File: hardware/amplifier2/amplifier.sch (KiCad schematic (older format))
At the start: 130 parts, among them IC1 AD8331, IC2 ISL55210, IC3 LP38798, IC4 NC7SVU04, IC5 LTC2252, J1 0, P1 5V, P2 UART, P4 VGA - LNA, P5 LNA - SDR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

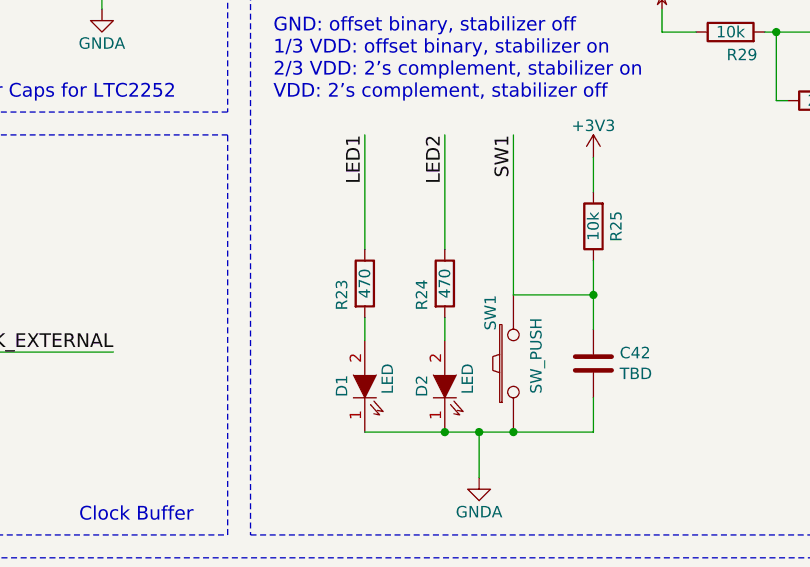
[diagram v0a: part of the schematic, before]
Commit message: Routed LDO, updated LED resistors, added resistor part numbers
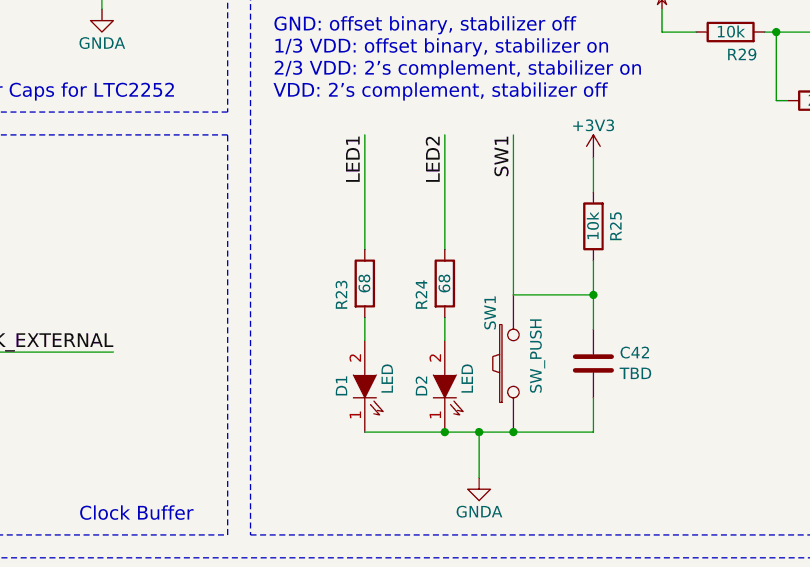
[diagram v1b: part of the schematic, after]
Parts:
- R23, R24: value 470 -> 68
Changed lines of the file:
@@
 P 7700 4250
 F 0 "R24" V 7600 4200 50  0000 C CNN
-F 1 "470" V 7700 4250 50  0000 C CNN
+F 1 "68" V 7700 4250 50  0000 C CNN
 F 2 "Resistors_SMD:R_0603" V 7630 4250 50  0001 C CNN
 F 3 "" H 7700 4250 50  0000 C CNN
@@
 P 7350 4250
 F 0 "R23" V 7250 4200 50  0000 C CNN
-F 1 "470" V 7350 4250 50  0000 C CNN
+F 1 "68" V 7350 4250 50  0000 C CNN
 F 2 "Resistors_SMD:R_0603" V 7280 4250 50  0001 C CNN
 F 3 "" H 7350 4250 50  0000 C CNN

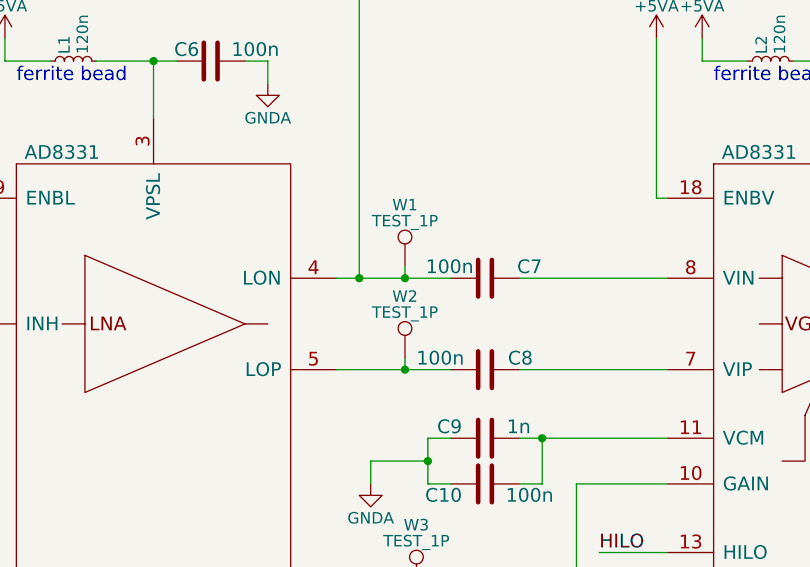
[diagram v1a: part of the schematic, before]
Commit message: everything done routing; removed obsolete testpins; needs groundplane checks and stitchings; needs mounting holes; maybe elaborate in schema
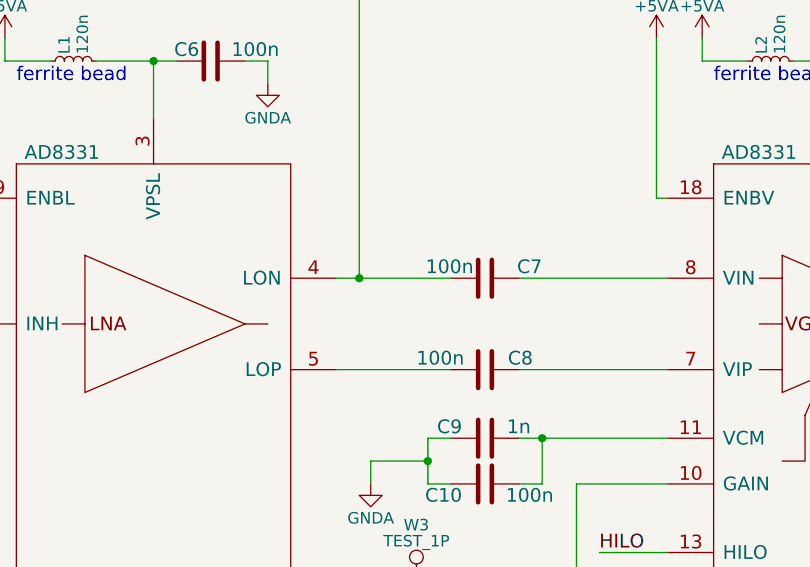
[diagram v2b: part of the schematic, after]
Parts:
- removed W1, W2: TEST_1P, Measurement_Points:Test_Point_Keystone_5005-5009_Compact, symbol TEST_1P
- C27: footprint Capacitors_SMD:C_0603 -> Capacitors_SMD:C_1210
- IC3: footprint (none) -> SDRfootprints:WSON12
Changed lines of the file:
@@
-$EndComp
-$Comp
-L TEST_1P W1
-U 1 1 580018C4
-P 3850 7450
-F 0 "W1" H 3850 7720 50  0000 C CNN
-F 1 "TEST_1P" H 3850 7650 50  0000 C CNN
-F 2 "Measurement_Points:Test_Point_Keystone_5005-5009_Compact" H 4050 7450 50  0001 C CNN
-F 3 "" H 4050 7450 50  0000 C CNN
-	1    3850 7450
-	1    0    0    -1
-$EndComp
-$Comp
-L TEST_1P W2
-U 1 1 58001975
-P 3850 7850
-F 0 "W2" H 3850 8120 50  0000 C CNN
-F 1 "TEST_1P" H 3850 8050 50  0000 C CNN
-F 2 "Measurement_Points:Test_Point_Keystone_5005-5009_Compact" H 4050 7850 50  0001 C CNN
-F 3 "" H 4050 7850 50  0000 C CNN
-	1    3850 7850
-	1    0    0    -1
 $EndComp
 $Comp
@@
 F 0 "C27" H 1565 1346 50  0000 L CNN
 F 1 "100u" H 1565 1255 50  0000 L CNN
-F 2 "Capacitors_SMD:C_0603" H 1488 1150 50  0001 C CNN
+F 2 "Capacitors_SMD:C_1210" H 1488 1150 50  0001 C CNN
 F 3 "" H 1450 1300 50  0000 C CNN
 	1    1450 1300
@@
 	8800 6050 8800 6500
 Connection ~ 8800 6150
-Wire Wire Line
-	3850 7450 3850 7500
-Connection ~ 3850 7500
-Wire Wire Line
-	3850 7850 3850 7900
-Connection ~ 3850 7900
 Wire Wire Line
 	9300 6150 9800 6150
@@
 F 0 "IC3" H 2875 2637 60  0000 C CNN
 F 1 "LP38798" H 2875 2531 60  0000 C CNN
-F 2 "" H 2900 1700 60  0001 C CNN
+F 2 "SDRfootprints:WSON12" H 2900 1700 60  0001 C CNN
 F 3 "" H 2900 1700 60  0001 C CNN
 	1    2900 1700

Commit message: Added notes to schematic explaining some of the features; Adjusted dimension markers of the board
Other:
- note added: "All Datasheets and values of the corresponding circuitry have been checked.\nIn general existing value shave been kept, even tho there was some\ncorrections and some values could not be reproduced.\nThis will be one measurement task to test if the values are actually proper."
- note added: "An 8-bit DAC for gain regulation has been chosen.\nIt is programmed using I2C; an FPGA implementation is required.\nIf a higher resolution is needed, it can be upgraded to a 10- or 12-bit DAC.\nIf noise behavior is okay is to be tested since the datasheet didn’t tell much."
- note added: "Different components of the AFE are separated and can be connected\ntogether through the external plugs. For differential signals\nnormal screw terminals were chosen to be used with a twisted pair cable.\nFor unbalanced signals BNC connectors were chosen."
- note added: "Every balanced (differential) signal has two output/input options.\nA balanced one and an unbalanced one if a balun was connected.\nThere is footprints for SMD baluns, but for optimal results and low cost,\nan external balun should be used.\n\n- To test more than one stage, chain stages together using connectors.\n- To test single stages, use in and output connectors directly."
- note added: "NOTES"
- note added: "Spare cap and resistor pads are included to be able\nto match the input impedance of the single components.\nThere is also jumpers added to disconnect the SMD baluns\nonce soldered in to avoid unwanted influences on the\nunbalanced transmission lines."
- note added: "The ADC part has also been included.\nIt has a groundplane as close as possible to the one in the app. note.\nAdiddionally the pre-ADC circuitry can now thoroughly be tested."

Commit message: minor fixes mr. hufschmid mentioned
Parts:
- T1, T2, T3, T4: footprint SDRfootprints:CX2041NLT -> SDRfootprints:T4-1-KK81
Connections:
- net IN2+: now also R38.1; no longer R37.1
- net IN2-: now also R37.1; no longer R38.1
- net OUT1+: now also R5.1; no longer R6.1
- net OUT1-: now also R6.1; no longer R5.1
- net OUT2+: now also R17.1; no longer R18.1
- net OUT2-: now also R18.1; no longer R17.1
